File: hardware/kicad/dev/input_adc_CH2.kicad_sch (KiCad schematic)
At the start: 90 parts, among them J201 BNC_Rosenberger, J201/2 Conn_01x01_Shielded, SW201 SW_DIP_x04, SW202 SW_DIP_x03, SW203 SW_DIP_x04, SW204 SW_DIP_x03, U201 AD8138ARZ, U202 AD9235

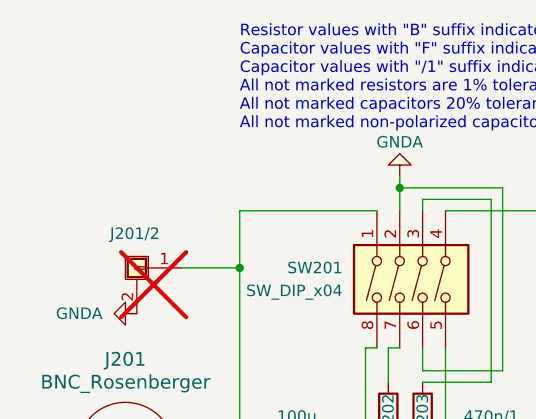
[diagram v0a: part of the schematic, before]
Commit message: repositioning of parts for more case options
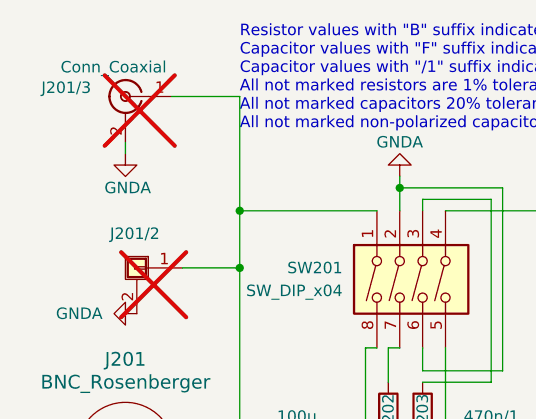
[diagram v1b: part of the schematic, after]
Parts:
- added J201/3: Conn_Coaxial, Connector_Coaxial:BNC_Amphenol_B6252HB-NPP3G-50_Horizontal, symbol Connector:Conn_Coaxial
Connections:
- net GNDA: now also J201/3.2 (Ext)
- net at C201.1, J201.1 (Signal), J201/2.1 (Pin_1)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: now also J201/3.1 (In)
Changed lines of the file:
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@@
 	)
 	(junction
+		(at 35.56 36.83)
+		(diameter 0)
+		(color 0 0 0 0)
+	)
+	(junction
 		(at 99.06 43.18)
 		(diameter 0)
@@
 	(wire
 		(pts
+			(xy 35.56 24.13) (xy 27.94 24.13)
+		)
+		(stroke
+			(width 0)
+			(type default)
+		)
+	)
+	(wire
+		(pts
 			(xy 149.86 73.66) (xy 154.94 73.66)
 		)
@@
 	(wire
 		(pts
+			(xy 35.56 36.83) (xy 35.56 24.13)
+		)
+		(stroke
+			(width 0)
+			(type default)
+		)
+	)
+	(wire
+		(pts
 			(xy 109.22 48.26) (xy 111.76 48.26)
 		)
@@
 	(wire
 		(pts
+			(xy 22.86 29.21) (xy 22.86 30.48)
+		)
+		(stroke
+			(width 0)
+			(type default)
+		)
+	)
+	(wire
+		(pts
 			(xy 99.06 81.28) (xy 99.06 71.12)
 		)
@@
 	)
 	(symbol
+		(lib_id "Connector:Conn_Coaxial")
+		(at 22.86 24.13 0)
+		(mirror y)
+		(unit 1)
+		(exclude_from_sim no)
+		(in_bom yes)
+		(on_board yes)
+		(dnp yes)
+		(property "Reference" "J201/3"
+			(at 19.05 23.1531 0)
+			(effects
+				(font
+					(size 1.27 1.27)
+				)
+				(justify left)
+			)
+		)
+		(property "Value" "Conn_Coaxial"
+			(at 27.432 20.8671 0)
+			(effects
+				(font
+					(size 1.27 1.27)
+				)
+				(justify left)
+			)
+		)
+		(property "Footprint" "Connector_Coaxial:BNC_Amphenol_B6252HB-NPP3G-50_Horizontal"
+			(at 22.86 24.13 0)
+			(effects
+				(font
+					(size 1.27 1.27)
+				)
+				(hide yes)
+			)
+		)
+		(property "Datasheet" "~"
+			(at 22.86 24.13 0)
+			(effects
+				(font
+					(size 1.27 1.27)
+				)
+				(hide yes)
+			)
+		)
+		(property "Description" "coaxial connector (BNC, SMA, SMB, SMC, Cinch/RCA, LEMO, ...)"
+			(at 22.86 24.13 0)
+			(effects
+				(font
+					(size 1.27 1.27)
+				)
+				(hide yes)
+			)
+		)
+		(pin "2"
+		)
+		(pin "1"
+		)
+		(instances
+			(project "misrc_v2.5"
+				(path "/bc796fa4-76ff-4554-a44c-2597c6c5788e/56b32eea-16d3-46c8-8e85-f12b91596617"
+					(reference "J201/3")
+					(unit 1)
+				)
+			)
+		)
+	)
+	(symbol
 		(lib_id "Device:C")
 		(at 252.73 39.37 0)
@@
 					(unit 1)
 				)
+			)
+		)
+	)
+	(symbol
+		(lib_id "power:GNDA")
+		(at 22.86 30.48 0)
+		(unit 1)
+		(exclude_from_sim no)
+		(in_bom yes)
+		(on_board yes)
+		(dnp no)
+		(property "Reference" "#PWR066"
+			(at 22.86 36.83 0)
+			(effects
+				(font
+					(size 1.27 1.27)
+				)
+				(hide yes)
+			)
+		)
+		(property "Value" "GNDA"
+			(at 23.114 34.29 0)
+			(effects
+				(font
+					(size 1.27 1.27)
+				)
+			)
+		)
+		(property "Footprint" ""
+			(at 22.86 30.48 0)
+			(effects
+				(font
+					(size 1.27 1.27)
+				)
+				(hide yes)
+			)
+		)
+		(property "Datasheet" ""
+			(at 22.86 30.48 0)
+			(effects
+				(font
+					(size 1.27 1.27)
+				)
+				(hide yes)
+			)
+		)
+		(property "Description" ""
+			(at 22.86 30.48 0)
+			(effects
+				(font
+					(size 1.27 1.27)
+				)
+				(hide yes)
+			)
+		)
+		(pin "1"
+		)
+		(instances
+			(project "misrc_v2.5"
+				(path "/bc796fa4-76ff-4554-a44c-2597c6c5788e/56b32eea-16d3-46c8-8e85-f12b91596617"
+					(reference "#PWR066")
+					(unit 1)
+				)
